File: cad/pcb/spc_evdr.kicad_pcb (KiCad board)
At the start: 2 copper layers, 237.6 x 100.5 mm, 120 parts, among them J1 BL_CONN, SW1 SW_Push, SW10 SW_Push, SW11 SW_Push, SW12 SW_Push, SW13 ON_OFF, SW14 SW_Push, SW15 SW_Push, SW16 SW_Push, SW17 SW_Push, SW18 SW_Push, SW19 SW_Push, SW2 SW_Push, SW20 SW_Push, SW21 SW_Push, SW22 SW_Push, SW23 SW_Push, SW24 SW_Push, SW25 SW_Push, SW26 SW_Push, SW27 SW_Push, SW28 SW_Push, SW29 SW_Push, SW3 SW_Push, SW30 SW_Push, SW31 SW_Push, SW32 SW_Push, SW33 SW_Push, SW34 SW_Push, SW35 SW_Push, SW36 SW_Push, SW37 SW_Push, SW38 SW_Push, SW39 SW_Push, SW4 SW_Push, SW40 SW_Push, SW41 SW_Push, SW42 SW_Push, SW43 SW_Push, SW44 SW_Push, SW45 SW_Push, SW46 SW_Push, SW47 SW_Push, SW48 SW_Push, SW49 SW_Push, SW5 RotaryEncoder_Switch, SW50 SW_Push, SW51 SW_Push, SW52 SW_Push, SW53 SW_Push, SW54 SKRHAAE010, SW6 SW_Push, SW7 SW_Push, SW8 SW_Push, SW9 SW_Push, U1 PCA9555PW, U2 xiao-ble, U3 Pimoroni haptic buzz

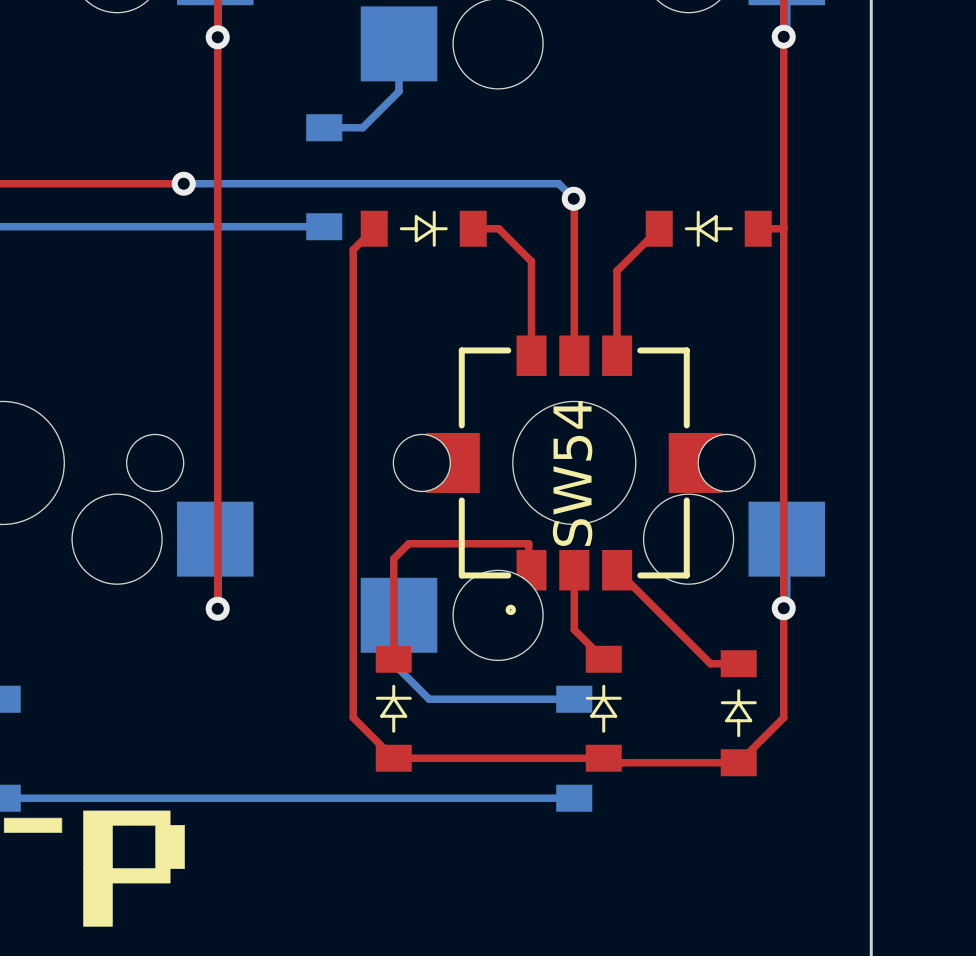
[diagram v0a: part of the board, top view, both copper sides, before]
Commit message: more hand soldering space around switch
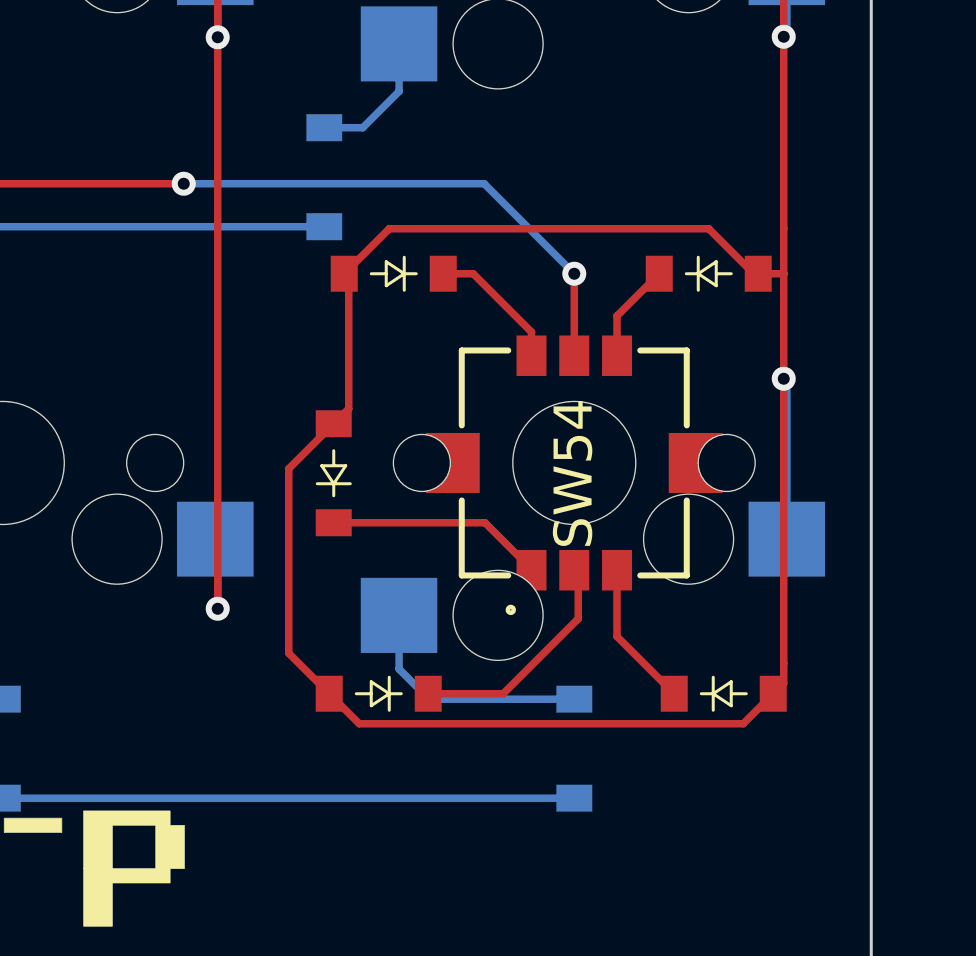
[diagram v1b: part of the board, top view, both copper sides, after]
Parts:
- moved D48 8.10 mm to (242.0, 123.7), turned to 90 degrees
- moved D49 7.52 mm to (243.5, 131.0), turned to 180 degrees
- moved D51 1.80 mm to (244.0, 117.0)
- moved D52 1.50 mm to (254.5, 117.0)
- moved D50 0.82 mm to (255.0, 131.0), turned to 0 degrees
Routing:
- net Col_11: track 214.5 -> 231.0 mm
- net Net-(D49-K): track 3.37 -> 7.71 mm
- net Net-(D48-K): track 8.97 -> 7.26 mm
- net Net-(D52-K): track 4.82 -> 3.32 mm
- net Row_0: track 165.8 -> 164.4 mm
- net Net-(D51-K): track 5.53 -> 4.54 mm

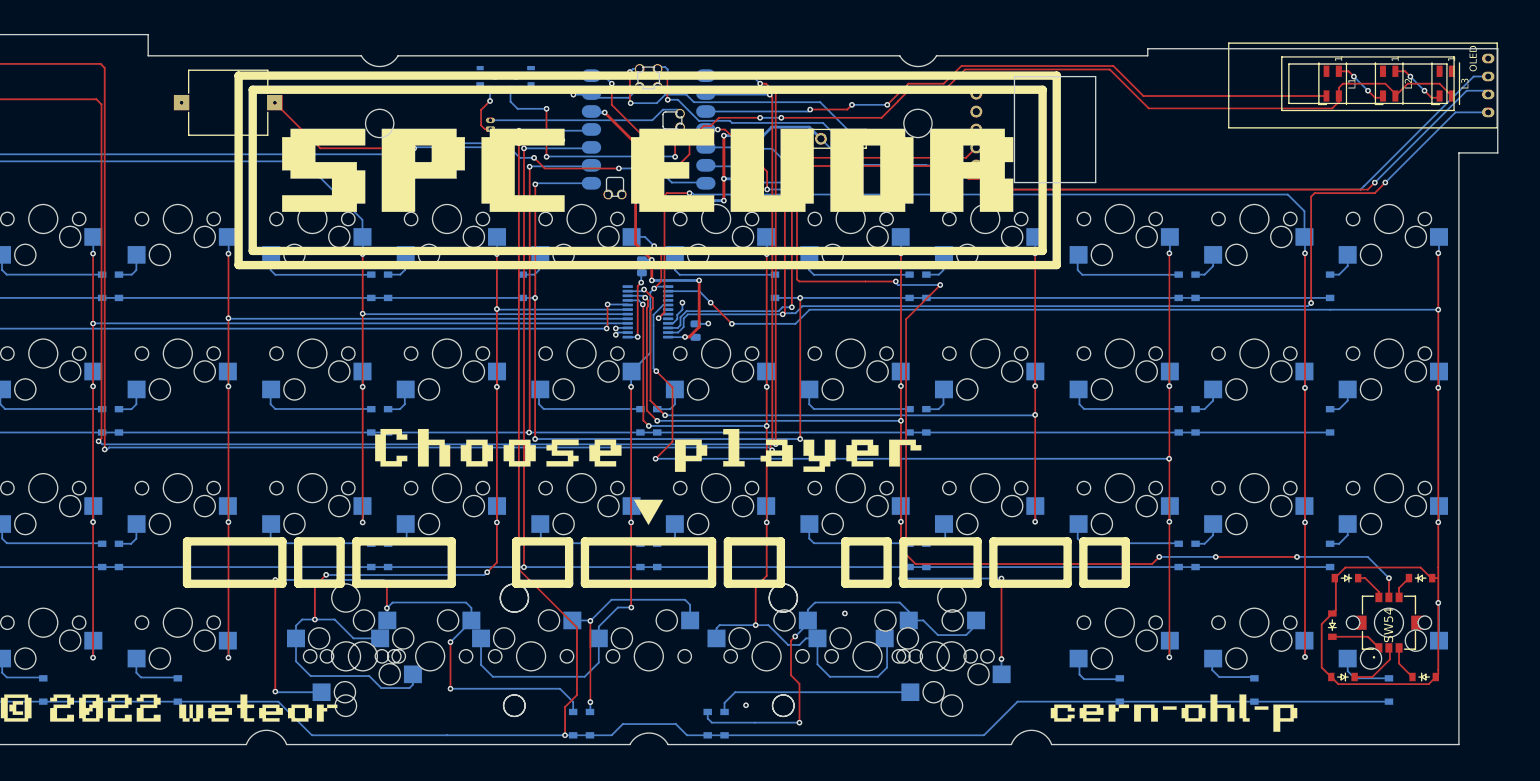
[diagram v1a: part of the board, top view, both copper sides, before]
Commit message: 12 col kicad files
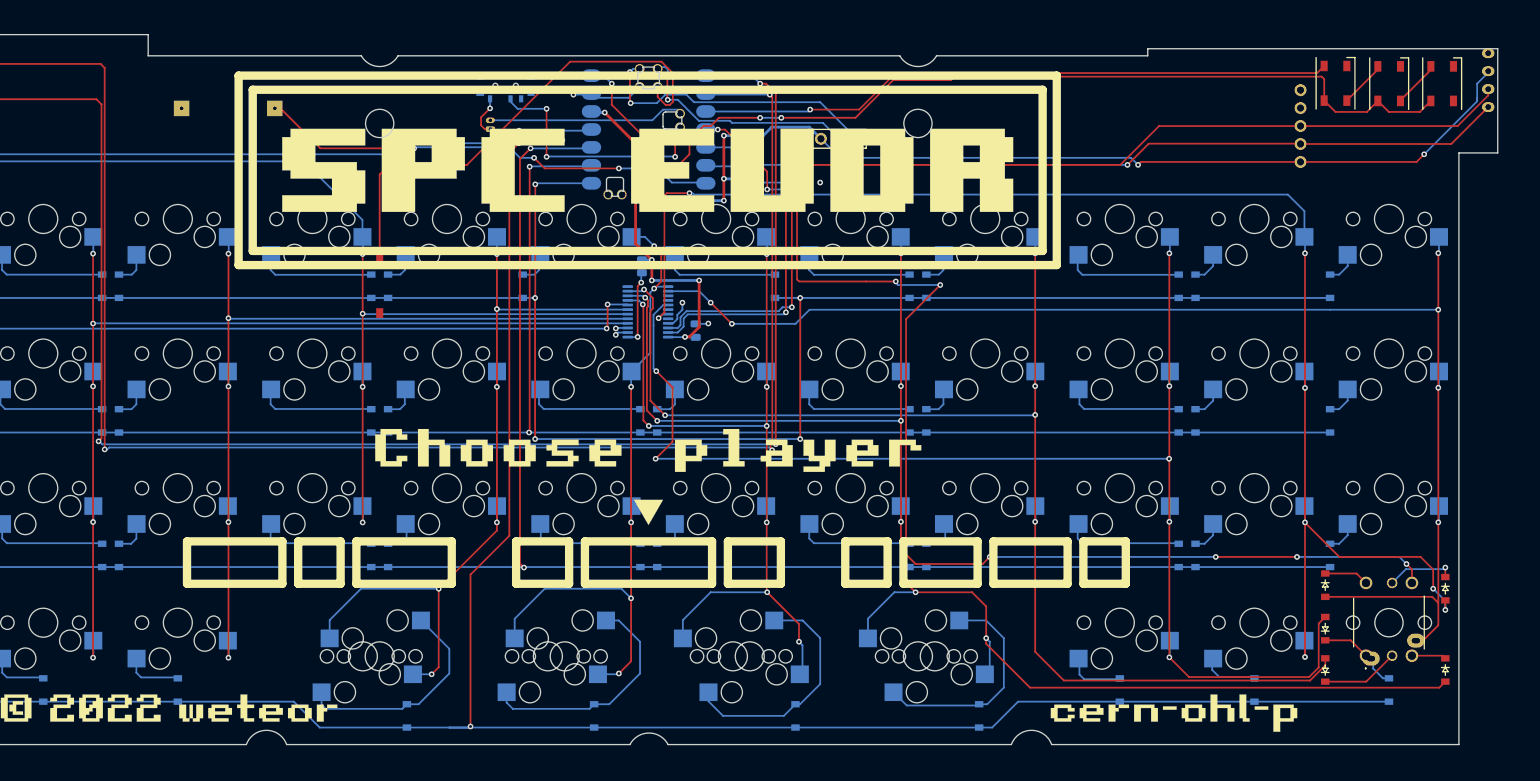
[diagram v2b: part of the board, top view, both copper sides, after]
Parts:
- D1, D10, D11, D12, D13, D14, D15, D16, D17, D18, D19, D2, D20, D21, D22, D23, D24, D25, D26, D27, D28, D29, D3, D30, D31, D32, D33, D34, D35, D36, D37, D38, D4, D40, D41, D42, D43, D44, D45, D46, D47, D5, D6, D7, D8, D9: value D -> 1N4148W
- D39: value D_Small -> 1N4148W
- D48, D49, D50, D51, D52: value ~ -> 1N4148W
- L1, L2, L3: value SK6812MINI -> SK6812; footprint LED_SMD:LED_SK6812MINI_PLCC4_3.5x3.5mm_P1.75mm -> LED_SMD:LED_SK6812_PLCC4_5.0x5.0mm_P3.2mm
- OL1: moved to B.Cu
- SW42, SW45: footprint weteor:CherryMX_Hotswap -> weteor:Inv_CherryMX_Hotswap_1.25u
- SW43, SW44: footprint weteor:CherryMX_Hotswap_1.75u -> weteor:Inv_CherryMX_Hotswap_1.5u
- SW48: footprint weteor:CherryMX_Hotswap -> kbd:CherryMX_1u
- SW49, SW51: footprint weteor:CherryMX_Hotswap_1.25u -> weteor:Inv_CherryMX_Hotswap_1.25u
- SW5: value RotaryEncoder_Switch -> EC11
- SW50: footprint weteor:CherryMX_Hotswap_3u_stabs -> weteor:Inv_CherryMX_Hotswap_1.5u
- SW52: footprint weteor:CherryMX_Hotswap_2.25u_stabs -> weteor:Inv_CherryMX_Hotswap_1.5u
- SW53: footprint weteor:CherryMX_Hotswap_2.25u_stabs -> weteor:Micro_Push_Button_3x6x2.5mm
- SW54: value SKRHAAE010 -> SKQUCAA010; footprint mouser:SKRHAAE010 -> mouser:SKQUCAA010
- U3: moved to F.Cu
- moved SW53 86.7 mm to (107.1, 75.7), turned to -90 degrees
- moved SW52 69.1 mm to (183.3, 128.1)
- moved SW50 38.1 mm to (107.1, 128.1)
- moved D44 36.1 mm to (192.0, 136.5)
- moved SW42 31.0 mm to (133.3, 128.1)
- moved SW45 31.0 mm to (157.1, 128.1), turned to 0 degrees
- moved U3 25.1 mm to (227.1, 53.0)
- moved D41 23.6 mm to (111.0, 136.5)
- moved D43 12.5 mm to (166.0, 136.5)
- moved SW54 5.69 mm to (246.8, 128.0)
- moved D52 3.81 mm to (258.0, 118.5), turned to -90 degrees
- moved D50 3.16 mm to (258.0, 130.0), turned to -90 degrees
- moved D51 3.16 mm to (241.0, 118.0), turned to -90 degrees
- moved D49 2.69 mm to (241.0, 130.0), turned to 90 degrees
- moved SW43 2.38 mm to (131.0, 128.1), turned to 180 degrees
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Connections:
- BT1 pad 2: Net-(BT1--) -> GND
- D48 pad 2: Col_11 -> Col_9
- D49 pad 2: Col_11 -> Col_8
- D50 pad 2: Col_11 -> Col_7
- D52 pad 2: Col_11 -> Col_10
- L1 pad 1: Net-(L1-DOUT) -> GND
- L1 pad 2: GND -> LED
- L1 pad 3: LED -> +5V
- L1 pad 4: +5V -> Net-(L1-DOUT)
- L2 pad 1: Net-(L2-DOUT) -> GND
- L2 pad 2: GND -> Net-(L1-DOUT)
- L2 pad 3: Net-(L1-DOUT) -> +5V
- L2 pad 4: +5V -> Net-(L2-DOUT)
- L3 pad 1: unconnected-(L3-DOUT-Pad1) -> GND
- L3 pad 2: GND -> Net-(L2-DOUT)
- L3 pad 3: Net-(L2-DOUT) -> +5V
- L3 pad 4: +5V -> unconnected-(L3-DOUT-Pad4)
- SW42 pad 1: Col_4 -> Col_5
- SW42 pad 2: Net-(D41-A) -> Net-(D42-A)
- SW45 pad 1: Col_7 -> Col_6
- SW45 pad 2: Net-(D44-A) -> Net-(D43-A)
- SW50 pad 1: Col_5 -> Col_4
- SW50 pad 2: Net-(D42-A) -> Net-(D41-A)
- SW51 pad 1: Col_6 -> Col_7
- SW51 pad 2: Net-(D43-A) -> Net-(D44-A)
- SW52 pad 1: Col_4 -> Col_7
- SW52 pad 2: Net-(D41-A) -> Net-(D44-A)
- SW53 pad 1: Col_6 -> rst
- SW53 pad 2: Net-(D43-A) -> GND
- SW54 pad 4: Net-(D51-K) -> Row_0
- SW54 pad 5: Row_0 -> Net-(D52-K)
- SW54 pad 6: Net-(D52-K) -> Net-(D51-K)
- U2 pad 17: unconnected-(U2-RESET-Pad17) -> rst
- U2 pad 20: Net-(BT1--) -> GND
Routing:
- net Col_7: track 135.9 -> 211.6 mm, vias 9 -> 8
- net rst: track 0.00 -> 69.1 mm
- net Col_8: track 118.9 -> 182.0 mm
- net Net-(D41-A): track 88.5 -> 31.3 mm, vias 6 -> 0
- net sda: track 199.9 -> 154.2 mm, vias 4 -> 3
- net Col_11: track 231.0 -> 191.6 mm, vias 7 -> 6
- net Col_9: track 164.2 -> 194.6 mm
- net Col_10: track 180.9 -> 209.6 mm, vias 6 -> 8
- net Col_4: track 139.1 -> 111.2 mm, vias 7 -> 6
- net Net-(BT1--): track 27.9 -> 0.00 mm
- net GND: track 19.2 -> 47.1 mm, vias 9 -> 7
- net Net-(D43-A): track 59.8 -> 33.9 mm, vias 2 -> 0
- net Col_6: track 133.0 -> 121.3 mm, vias 7 -> 8
- net scl: track 168.1 -> 158.0 mm, vias 3 -> 2
- net Net-(D52-K): track 3.32 -> 9.79 mm, vias 0 -> 1
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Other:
- outline, holes or cut-outs redrawn

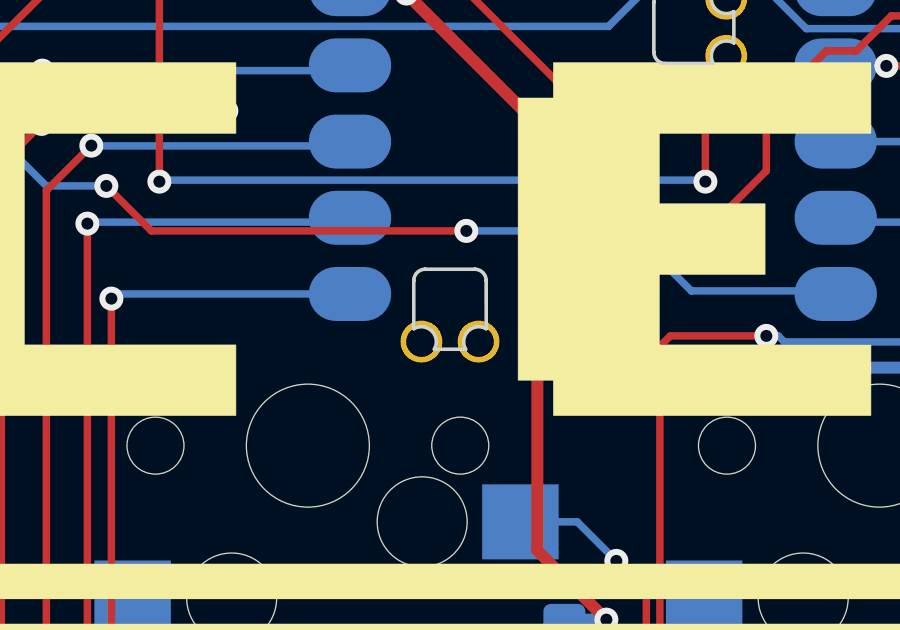
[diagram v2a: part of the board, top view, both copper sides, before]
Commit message: reorganized and fix silkscreens
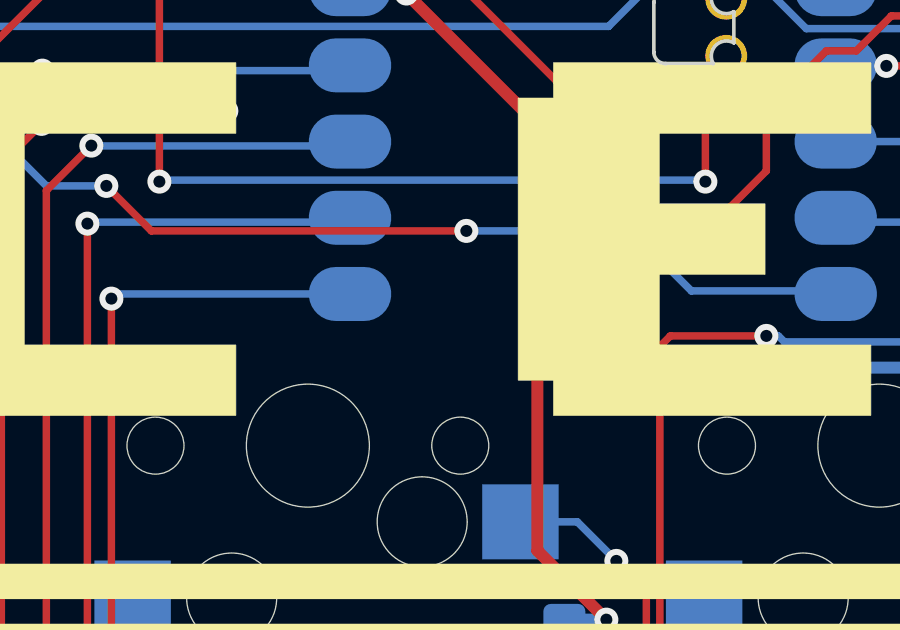
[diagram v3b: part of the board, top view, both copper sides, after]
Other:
- board text added: "3V3"
- board text added: "GND"
- board text added: "OFF"
- board text added: "ON"
- board text added: "bat +"
- board text added: "bat -"
- board text added: "scl"
- board text added: "sda"
- board text added: "swclk"
- board text added: "swdio"
